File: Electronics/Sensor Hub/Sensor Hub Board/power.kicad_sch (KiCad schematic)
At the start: 25 parts, among them IC201 TPS54295PWPR, J2 Screw_Terminal_01x02, J202 Conn_01x02_Pin, J203 Conn_01x02_Pin, J204 Conn_01x02_Pin

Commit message: PCB Schematics finished
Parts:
- added J205: Conn_01x02_Pin, Connector_PinHeader_2.54mm:PinHeader_1x02_P2.54mm_Vertical, symbol Connector:Conn_01x02_Pin
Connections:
- net +3V3: now also J204.1 (Pin_1), J205.1 (Pin_1)
- net +5V: no longer J204.1 (Pin_1)
- net GND: now also J205.2 (Pin_2)
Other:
- note added: "3.3V Headers"
- moved on the sheet: D1, J2, J202, J203, J204

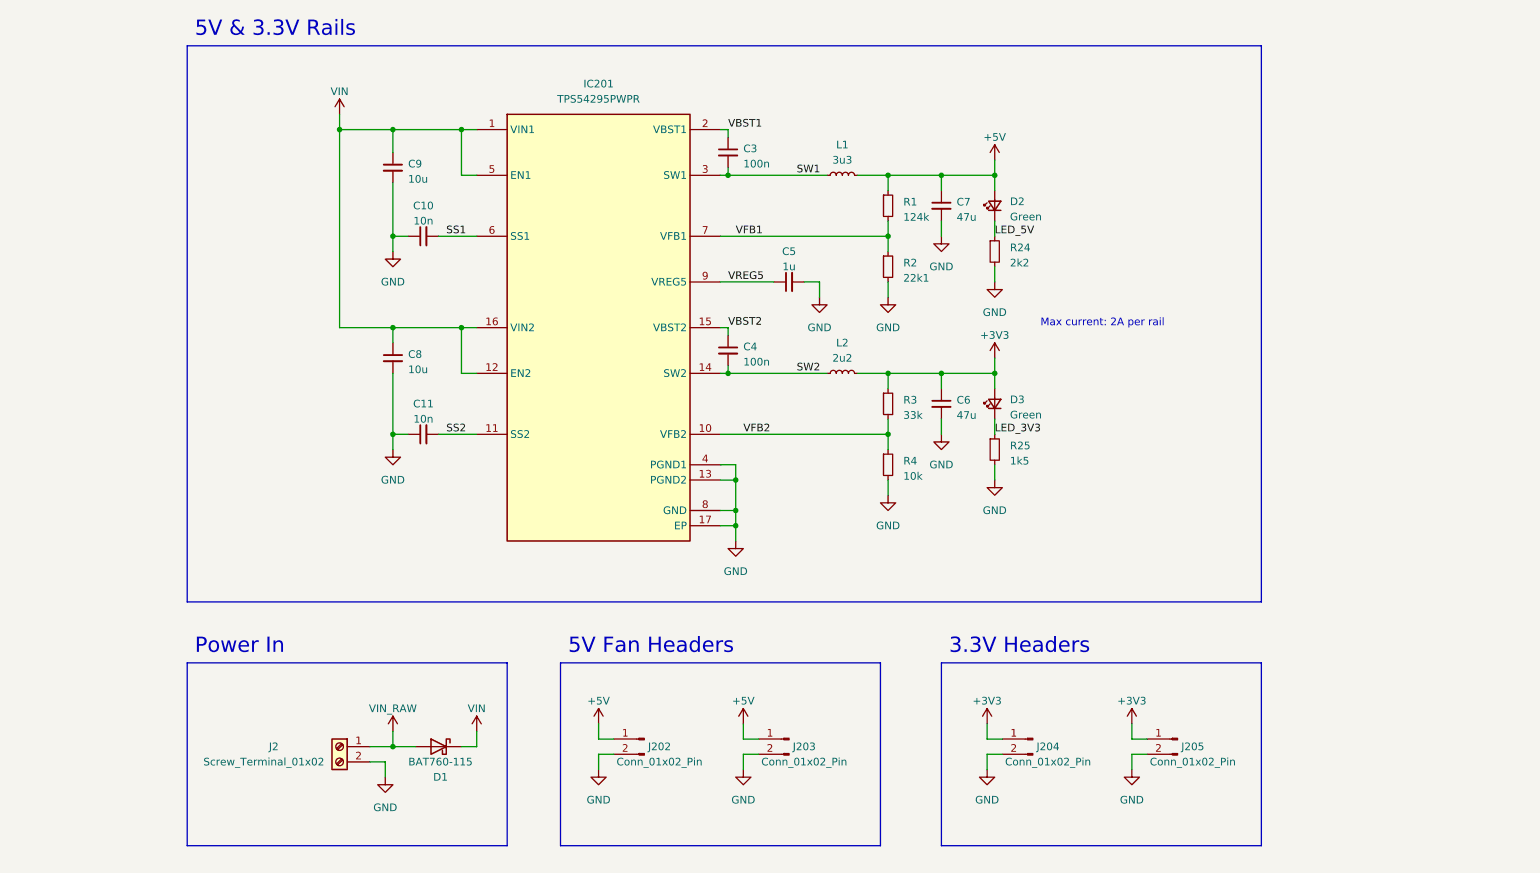
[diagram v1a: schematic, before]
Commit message: Schematic updates
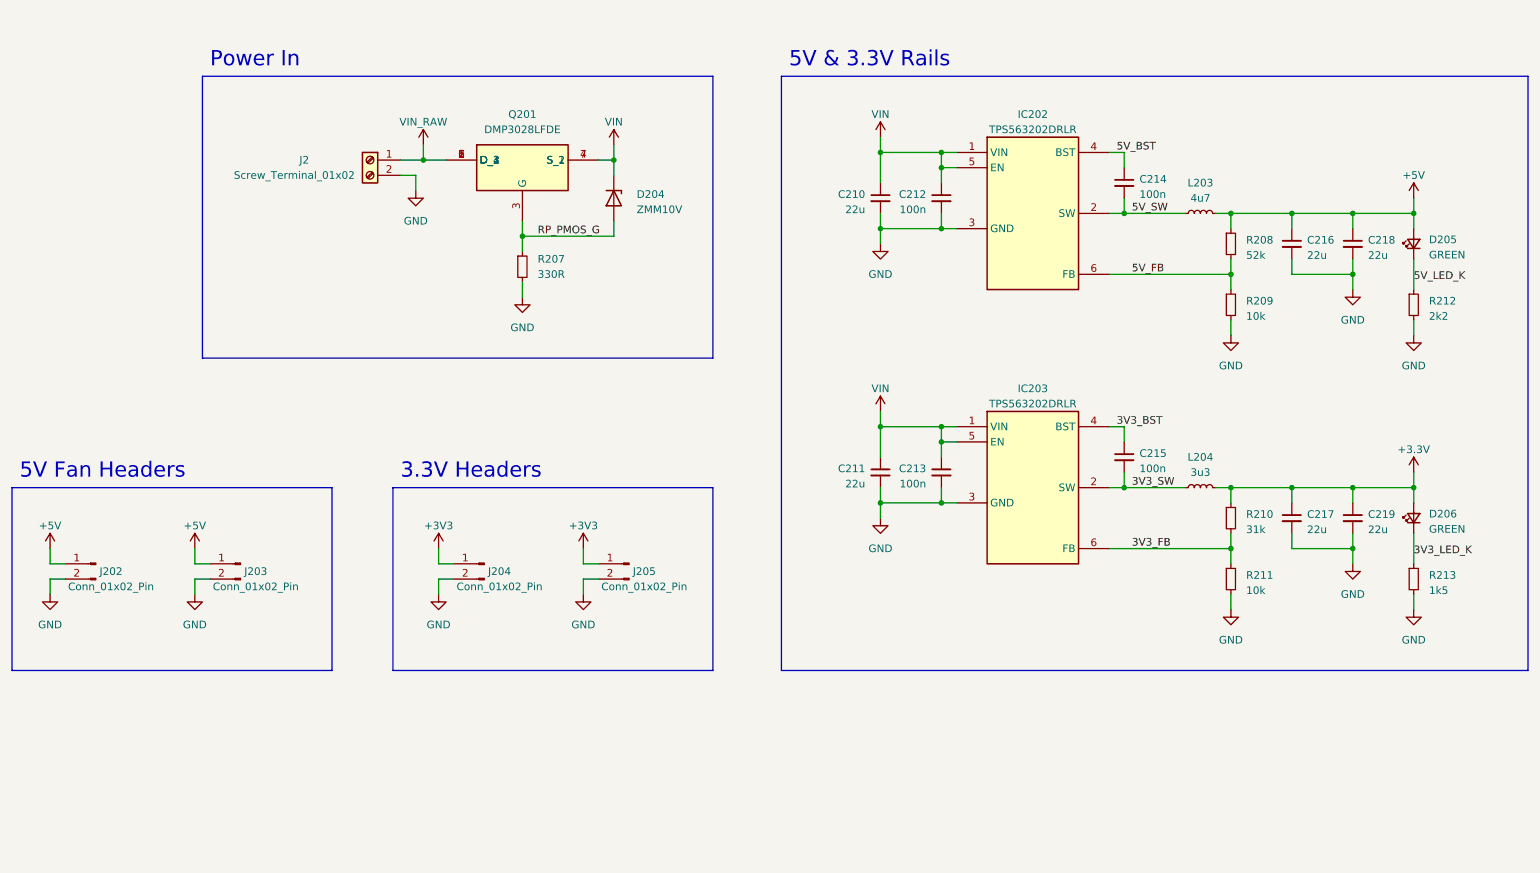
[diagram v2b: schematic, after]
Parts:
- removed C10, C11: 10n, Capacitor_SMD:C_0402_1005Metric, symbol Device:C_Small
- removed C3, C4: 100n, Capacitor_SMD:C_0402_1005Metric, symbol Device:C_Small
- removed C5: 1u, Capacitor_SMD:C_0402_1005Metric, symbol Device:C_Small
- removed C6, C7: 47u, Capacitor_SMD:C_0805_2012Metric, symbol Device:C_Small
- removed C8, C9: 10u, Capacitor_SMD:C_0603_1608Metric, symbol Device:C_Small
- removed D1: BAT760-115, Diode_SMD:D_SOD-323, symbol Device:D_Schottky
- removed D2, D3: Green, LED_SMD:LED_0603_1608Metric, symbol Device:LED_Small
- removed IC201: TPS54295PWPR, SOP65P640X120-17N, symbol TPS54295PWPR:TPS54295PWPR
- removed L1: 3u3, MSL Footprints:29332C, symbol Device:L_Small
- removed L2: 2u2, MSL Footprints:29222C, symbol Device:L_Small
- removed R1: 124k, Resistor_SMD:R_0402_1005Metric, symbol Device:R_Small
- removed R2: 22k1, Resistor_SMD:R_0402_1005Metric, symbol Device:R_Small
- removed R24: 2k2, Resistor_SMD:R_0402_1005Metric, symbol Device:R_Small
- removed R25: 1k5, Resistor_SMD:R_0402_1005Metric, symbol Device:R_Small
- removed R3: 33k, Resistor_SMD:R_0402_1005Metric, symbol Device:R_Small
- removed R4: 10k, Resistor_SMD:R_0402_1005Metric, symbol Device:R_Small
- added C210, C211, C216, C217, C218, C219: 22u, Capacitor_SMD:C_0603_1608Metric, symbol Device:C_Small
- added C212, C213, C214, C215: 100n, Capacitor_SMD:C_0402_1005Metric, symbol Device:C_Small
- added D204: ZMM10V, Diode_SMD:D_MiniMELF, symbol Diode:ZMMxx
- added D205, D206: GREEN, LED_SMD:LED_0603_1608Metric, symbol Device:LED_Small
- added IC202, IC203: TPS563202DRLR, MSL Footprints:SOTFL50P160X60-6N, symbol TPS563202DRLR:TPS563202DRLR
- added L203: 4u7, Inductor_SMD:L_Chilisin_BMRA00040420, symbol Device:L_Small
- added L204: 3u3, Inductor_SMD:L_Chilisin_BMRA00040420, symbol Device:L_Small
- added Q201: DMP3028LFDE, MSL Footprints:DMP2066UFDE7, symbol DMP3028LFDE-7:DMP3028LFDE
- added R207: 330R, Resistor_SMD:R_0402_1005Metric, symbol Device:R_Small
- added R208: 52k, Resistor_SMD:R_0402_1005Metric, symbol Device:R_Small
- added R209, R211: 10k, Resistor_SMD:R_0402_1005Metric, symbol Device:R_Small
- added R210: 31k, Resistor_SMD:R_0402_1005Metric, symbol Device:R_Small
- added R212: 2k2, Resistor_SMD:R_0402_1005Metric, symbol Device:R_Small
- added R213: 1k5, Resistor_SMD:R_0402_1005Metric, symbol Device:R_Small
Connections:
- net +5V: now also C216.1, C218.1, D205.2 (A), L203.2, R208.1
- net GND: now also C210.2, C211.2, C212.2, C213.2, C216.2, C217.2, C218.2, C219.2, IC202.3 (GND), IC203.3 (GND), R207.2, R209.2, R211.2, R212.2, R213.2
- net VIN: now also C210.1, C211.1, C212.1, C213.1, D204.1 (K), IC202.1 (VIN), IC202.5 (EN), IC203.1 (VIN), IC203.5 (EN), Q201.4 (S_1), Q201.7 (S_2)
- net VIN_RAW: now also Q201.1 (D_1), Q201.2 (D_2), Q201.5 (D_3), Q201.6 (D_4)
- new net +3.3V: C217.1, C219.1, D206.2 (A), L204.2, R210.1
- new net 3V3_BST: C215.1, IC203.4 (BST)
- new net 3V3_FB: IC203.6 (FB), R210.2, R211.1
- new net 3V3_LED_K: D206.1 (K), R213.1
- new net 3V3_SW: C215.2, IC203.2 (SW), L204.1
- new net 5V_BST: C214.1, IC202.4 (BST)
- new net 5V_FB: IC202.6 (FB), R208.2, R209.1
- new net 5V_LED_K: D205.1 (K), R212.1
- new net 5V_SW: C214.2, IC202.2 (SW), L203.1
- new net RP_PMOS_G: D204.2 (A), Q201.3 (G), R207.1
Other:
- note removed: "Max current: 2A per rail"
- moved on the sheet: J202, J203, J204, J205

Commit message: Gateway board layout complete and routing begun
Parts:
- removed J2: Screw_Terminal_01x02, TerminalBlock:TerminalBlock_bornier-2_P5.08mm, symbol Connector:Screw_Terminal_01x02
- removed J202, J203, J204, J205: Conn_01x02_Pin, Connector_PinHeader_2.54mm:PinHeader_1x02_P2.54mm_Vertical, symbol Connector:Conn_01x02_Pin
- added J201, J202, J203, J204: JST-XH-2.50mm, Connector_JST:JST_XH_B2B-XH-A_1x02_P2.50mm_Vertical, symbol MSL_Symbols:JST_2.5mm_1x2
- added J207: Pluggable_Terminal_01x02, MSL Footprints:Pluggable_terminal-2_P5.08mm, symbol MSL_Symbols:Pluggable_Terminal_01x02
- R207: value 330R -> 4k7
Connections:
- net +3V3: now also J202.1 (Pin_1), J204.1 (Pin_1)
- net +5V: now also J201.1 (Pin_1), J203.1 (Pin_1)
- net GND: now also J201.2 (Pin_2), J202.2 (Pin_2), J203.2 (Pin_2), J204.2 (Pin_2), J207.2 (Pin_2)
- net VIN_RAW: now also J207.1 (Pin_1)
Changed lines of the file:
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@@
       (effects (font (size 1.27 1.27)) (justify left))
     )
-    (property "Value" "330R" (at 109.22 63.5 0)
+    (property "Value" "4k7" (at 109.22 63.5 0)
       (effects (font (size 1.27 1.27)) (justify left))
     )
@@
     )
   )
-  (symbol (lib_id "Connector:Screw_Terminal_01x02") (at 81.28 44.45 0) (mirror y) (unit 1)
-    (in_bom yes) (on_board yes) (dnp no)
-    (property "Reference" "J2" (at 71.12 44.45 0)
-      (effects (font (size 1.27 1.27)) (justify left))
-    )
-    (property "Value" "Screw_Terminal_01x02" (at 78.74 46.99 0)
-      (effects (font (size 1.27 1.27)) (justify left))
-    )
-    (property "Footprint" "TerminalBlock:TerminalBlock_bornier-2_P5.08mm" (at 81.28 44.45 0)
-      (effects (font (size 1.27 1.27)) hide)
-    )
-    (property "Datasheet" "~" (at 81.28 44.45 0)
-      (effects (font (size 1.27 1.27)) hide)
-    )
-    (pin "1")
-    (pin "2")
-    (instances
-      (project "Sensor Hub Board"
-        (path "/5318664d-e328-4e84-a383-7318275dc447/86a04d6c-5487-4291-b767-6da69e96f7da"
-          (reference "J2") (unit 1)
-        )
-        (path "/5318664d-e328-4e84-a383-7318275dc447/2d8a1952-b517-4da6-9eec-185b726181fe"
-          (reference "J207") (unit 1)
-        )
-      )
-      (project "Power Board"
-        (path "/d8843e0a-fd8a-4193-ba57-f0164156e030/fab43204-4de8-48e9-a4c9-80bcd4a9c27a"
-          (reference "J5") (unit 1)
-        )
-      )
-    )
-  )
   (symbol (lib_id "power:GND") (at 52.07 116.84 0) (mirror y) (unit 1)
     (in_bom yes) (on_board yes) (dnp no) (fields_autoplaced)
@@
     )
   )
-  (symbol (lib_id "Connector:Conn_01x02_Pin") (at 100.33 111.76 0) (mirror y) (unit 1)
-    (in_bom yes) (on_board yes) (dnp no)
-    (property "Reference" "J204" (at 102.87 113.03 0)
-      (effects (font (size 1.27 1.27)))
-    )
-    (property "Value" "Conn_01x02_Pin" (at 102.87 115.57 0)
-      (effects (font (size 1.27 1.27)))
-    )
-    (property "Footprint" "Connector_PinHeader_2.54mm:PinHeader_1x02_P2.54mm_Vertical" (at 100.33 111.76 0)
-      (effects (font (size 1.27 1.27)) hide)
-    )
-    (property "Datasheet" "~" (at 100.33 111.76 0)
-      (effects (font (size 1.27 1.27)) hide)
-    )
-    (pin "1")
-    (pin "2")
-    (instances
-      (project "Sensor Hub Board"
-        (path "/5318664d-e328-4e84-a383-7318275dc447/2d8a1952-b517-4da6-9eec-185b726181fe"
-          (reference "J204") (unit 1)
-        )
-      )
-    )
-  )
   (symbol (lib_id "power:+5V") (at 255.27 50.8 0) (unit 1)
     (in_bom yes) (on_board yes) (dnp no) (fields_autoplaced)
@@
     )
   )
+  (symbol (lib_id "MSL_Symbols:JST_2.5mm_1x2") (at 59.69 113.03 0) (unit 1)
+    (in_bom yes) (on_board yes) (dnp no)
+    (property "Reference" "J201" (at 55.88 105.41 0)
+      (effects (font (size 1.27 1.27)) (justify left))
+    )
+    (property "Value" "JST-XH-2.50mm" (at 55.88 107.95 0)
+      (effects (font (size 1.27 1.27)) (justify left))
+    )
+    (property "Footprint" "Connector_JST:JST_XH_B2B-XH-A_1x02_P2.50mm_Vertical" (at 59.69 118.11 0)
+      (effects (font (size 1.27 1.27)) hide)
+    )
+    (property "Datasheet" "" (at 54.61 109.22 0)
+      (effects (font (size 1.27 1.27)) hide)
+    )
+    (pin "1")
+    (pin "2")
+    (instances
+      (project "Sensor Hub Board"
+        (path "/5318664d-e328-4e84-a383-7318275dc447/2d8a1952-b517-4da6-9eec-185b726181fe"
+          (reference "J201") (unit 1)
+        )
+      )
+    )
+  )
   (symbol (lib_id "Device:R_Small") (at 224.79 104.14 0) (unit 1)
     (in_bom yes) (on_board yes) (dnp no) (fields_autoplaced)
@@
         (path "/fc9ec853-be53-41ed-ad76-ff5f6d436e9e"
           (reference "C104") (unit 1)
-        )
-      )
-    )
-  )
-  (symbol (lib_id "Connector:Conn_01x02_Pin") (at 59.69 111.76 0) (mirror y) (unit 1)
-    (in_bom yes) (on_board yes) (dnp no)
-    (property "Reference" "J203" (at 62.23 113.03 0)
-      (effects (font (size 1.27 1.27)))
-    )
-    (property "Value" "Conn_01x02_Pin" (at 62.23 115.57 0)
-      (effects (font (size 1.27 1.27)))
-    )
-    (property "Footprint" "Connector_PinHeader_2.54mm:PinHeader_1x02_P2.54mm_Vertical" (at 59.69 111.76 0)
-      (effects (font (size 1.27 1.27)) hide)
-    )
-    (property "Datasheet" "~" (at 59.69 111.76 0)
-      (effects (font (size 1.27 1.27)) hide)
-    )
-    (pin "1")
-    (pin "2")
-    (instances
-      (project "Sensor Hub Board"
-        (path "/5318664d-e328-4e84-a383-7318275dc447/2d8a1952-b517-4da6-9eec-185b726181fe"
-          (reference "J203") (unit 1)
         )
       )
@@
     )
   )
+  (symbol (lib_id "MSL_Symbols:JST_2.5mm_1x2") (at 124.46 113.03 0) (unit 1)
+    (in_bom yes) (on_board yes) (dnp no)
+    (property "Reference" "J204" (at 120.65 105.41 0)
+      (effects (font (size 1.27 1.27)) (justify left))
+    )
+    (property "Value" "JST-XH-2.50mm" (at 120.65 107.95 0)
+      (effects (font (size 1.27 1.27)) (justify left))
+    )
+    (property "Footprint" "Connector_JST:JST_XH_B2B-XH-A_1x02_P2.50mm_Vertical" (at 124.46 118.11 0)
+      (effects (font (size 1.27 1.27)) hide)
+    )
+    (property "Datasheet" "" (at 119.38 109.22 0)
+      (effects (font (size 1.27 1.27)) hide)
+    )
+    (pin "1")
+    (pin "2")
+    (instances
+      (project "Sensor Hub Board"
+        (path "/5318664d-e328-4e84-a383-7318275dc447/2d8a1952-b517-4da6-9eec-185b726181fe"
+          (reference "J204") (unit 1)
+        )
+      )
+    )
+  )
+  (symbol (lib_id "MSL_Symbols:JST_2.5mm_1x2") (at 100.33 113.03 0) (unit 1)
+    (in_bom yes) (on_board yes) (dnp no)
+    (property "Reference" "J202" (at 96.52 105.41 0)
+      (effects (font (size 1.27 1.27)) (justify left))
+    )
+    (property "Value" "JST-XH-2.50mm" (at 96.52 107.95 0)
+      (effects (font (size 1.27 1.27)) (justify left))
+    )
+    (property "Footprint" "Connector_JST:JST_XH_B2B-XH-A_1x02_P2.50mm_Vertical" (at 100.33 118.11 0)
+      (effects (font (size 1.27 1.27)) hide)
+    )
+    (property "Datasheet" "" (at 95.25 109.22 0)
+      (effects (font (size 1.27 1.27)) hide)
+    )
+    (pin "1")
+    (pin "2")
+    (instances
+      (project "Sensor Hub Board"
+        (path "/5318664d-e328-4e84-a383-7318275dc447/2d8a1952-b517-4da6-9eec-185b726181fe"
+          (reference "J202") (unit 1)
+        )
+      )
+    )
+  )
+  (symbol (lib_id "MSL_Symbols:Pluggable_Terminal_01x02") (at 81.28 44.45 0) (mirror y) (unit 1)
+    (in_bom yes) (on_board yes) (dnp no) (fields_autoplaced)
+    (property "Reference" "J207" (at 81.28 39.37 0)
+      (effects (font (size 1.27 1.27)))
+    )
+    (property "Value" "Pluggable_Terminal_01x02" (at 81.28 41.91 0)
+      (effects (font (size 1.27 1.27)))
+    )
+    (property "Footprint" "MSL Footprints:Pluggable_terminal-2_P5.08mm" (at 81.28 44.45 0)
+      (effects (font (size 1.27 1.27)) hide)
+    )
+    (property "Datasheet" "~" (at 81.28 44.45 0)
+      (effects (font (size 1.27 1.27)) hide)
+    )
+    (pin "1")
+    (pin "2")
+    (instances
+      (project "Sensor Hub Board"
+        (path "/5318664d-e328-4e84-a383-7318275dc447/2d8a1952-b517-4da6-9eec-185b726181fe"
+          (reference "J207") (unit 1)
+        )
+      )
+    )
+  )
   (symbol (lib_id "power:GND") (at 88.9 49.53 0) (unit 1)
     (in_bom yes) (on_board yes) (dnp no) (fields_autoplaced)
@@
     )
   )
-  (symbol (lib_id "Connector:Conn_01x02_Pin") (at 35.56 111.76 0) (mirror y) (unit 1)
+  (symbol (lib_id "MSL_Symbols:JST_2.5mm_1x2") (at 35.56 113.03 0) (unit 1)
     (in_bom yes) (on_board yes) (dnp no)
-    (property "Reference" "J202" (at 38.1 113.03 0)
-      (effects (font (size 1.27 1.27)))
-    )
-    (property "Value" "Conn_01x02_Pin" (at 38.1 115.57 0)
-      (effects (font (size 1.27 1.27)))
-    )
-    (property "Footprint" "Connector_PinHeader_2.54mm:PinHeader_1x02_P2.54mm_Vertical" (at 35.56 111.76 0)
-      (effects (font (size 1.27 1.27)) hide)
-    )
-    (property "Datasheet" "~" (at 35.56 111.76 0)
-      (effects (font (size 1.27 1.27)) hide)
-    )
-    (pin "1")
-    (pin "2")
-    (instances
-      (project "Sensor Hub Board"
-        (path "/5318664d-e328-4e84-a383-7318275dc447/2d8a1952-b517-4da6-9eec-185b726181fe"
-          (reference "J202") (unit 1)
+    (property "Reference" "J203" (at 31.75 105.41 0)
+      (effects (font (size 1.27 1.27)) (justify left))
+    )
+    (property "Value" "JST-XH-2.50mm" (at 31.75 107.95 0)
+      (effects (font (size 1.27 1.27)) (justify left))
+    )
+    (property "Footprint" "Connector_JST:JST_XH_B2B-XH-A_1x02_P2.50mm_Vertical" (at 35.56 118.11 0)
+      (effects (font (size 1.27 1.27)) hide)
+    )
+    (property "Datasheet" "" (at 30.48 109.22 0)
+      (effects (font (size 1.27 1.27)) hide)
+    )
+    (pin "1")
+    (pin "2")
+    (instances
+      (project "Sensor Hub Board"
+        (path "/5318664d-e328-4e84-a383-7318275dc447/2d8a1952-b517-4da6-9eec-185b726181fe"
+          (reference "J203") (unit 1)
         )
       )
@@
         )
       )
-    )
-  )
-  (symbol (lib_id "Connector:Conn_01x02_Pin") (at 124.46 111.76 0) (mirror y) (unit 1)
-    (in_bom yes) (on_board yes) (dnp no)
-    (property "Reference" "J205" (at 127 113.03 0)
-      (effects (font (size 1.27 1.27)))
-    )
-    (property "Value" "Conn_01x02_Pin" (at 127 115.57 0)
-      (effects (font (size 1.27 1.27)))
-    )
-    (property "Footprint" "Connector_PinHeader_2.54mm:PinHeader_1x02_P2.54mm_Vertical" (at 124.46 111.76 0)
-      (effects (font (size 1.27 1.27)) hide)
-    )
-    (property "Datasheet" "~" (at 124.46 111.76 0)
-      (effects (font (size 1.27 1.27)) hide)
-    )
-    (pin "1")
-    (pin "2")
-    (instances
-      (project "Sensor Hub Board"
-        (path "/5318664d-e328-4e84-a383-7318275dc447/2d8a1952-b517-4da6-9eec-185b726181fe"
-          (reference "J205") (unit 1)
-        )
-      )

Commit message: Sensor hub board done
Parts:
- removed J201, J202, J203, J204: JST-XH-2.50mm, Connector_JST:JST_XH_B2B-XH-A_1x02_P2.50mm_Vertical, symbol MSL_Symbols:JST_2.5mm_1x2
- renumbered C210 to C201, C211 to C202, C212 to C203, C213 to C204, C214 to C205, C215 to C206, C216 to C207, C217 to C208, C218 to C209, C219 to C210, D204 to D201, D205 to D202, D206 to D203, IC202 to IC201, IC203 to IC202, J207 to J203, L203 to L201, L204 to L202, R207 to R201, R208 to R202, R209 to R203, R210 to R204, R211 to R205, R212 to R206, R213 to R207
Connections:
- net VIN_RAW: now also Q201.8 (D_5)
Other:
- note removed: "3.3V Headers"
- note removed: "5V Fan Headers"

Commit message: All boards done
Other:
- moved on the sheet: C201, C202, C203, C204, C205, C206, C207, C208, C209, C210, D201, D202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
